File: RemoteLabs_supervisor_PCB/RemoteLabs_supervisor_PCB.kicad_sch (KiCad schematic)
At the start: 20 parts, among them J1 Super_Prog_Header, J2 WS2821B Header, J26 Student_Prog_Header, J27 Analog Buffer

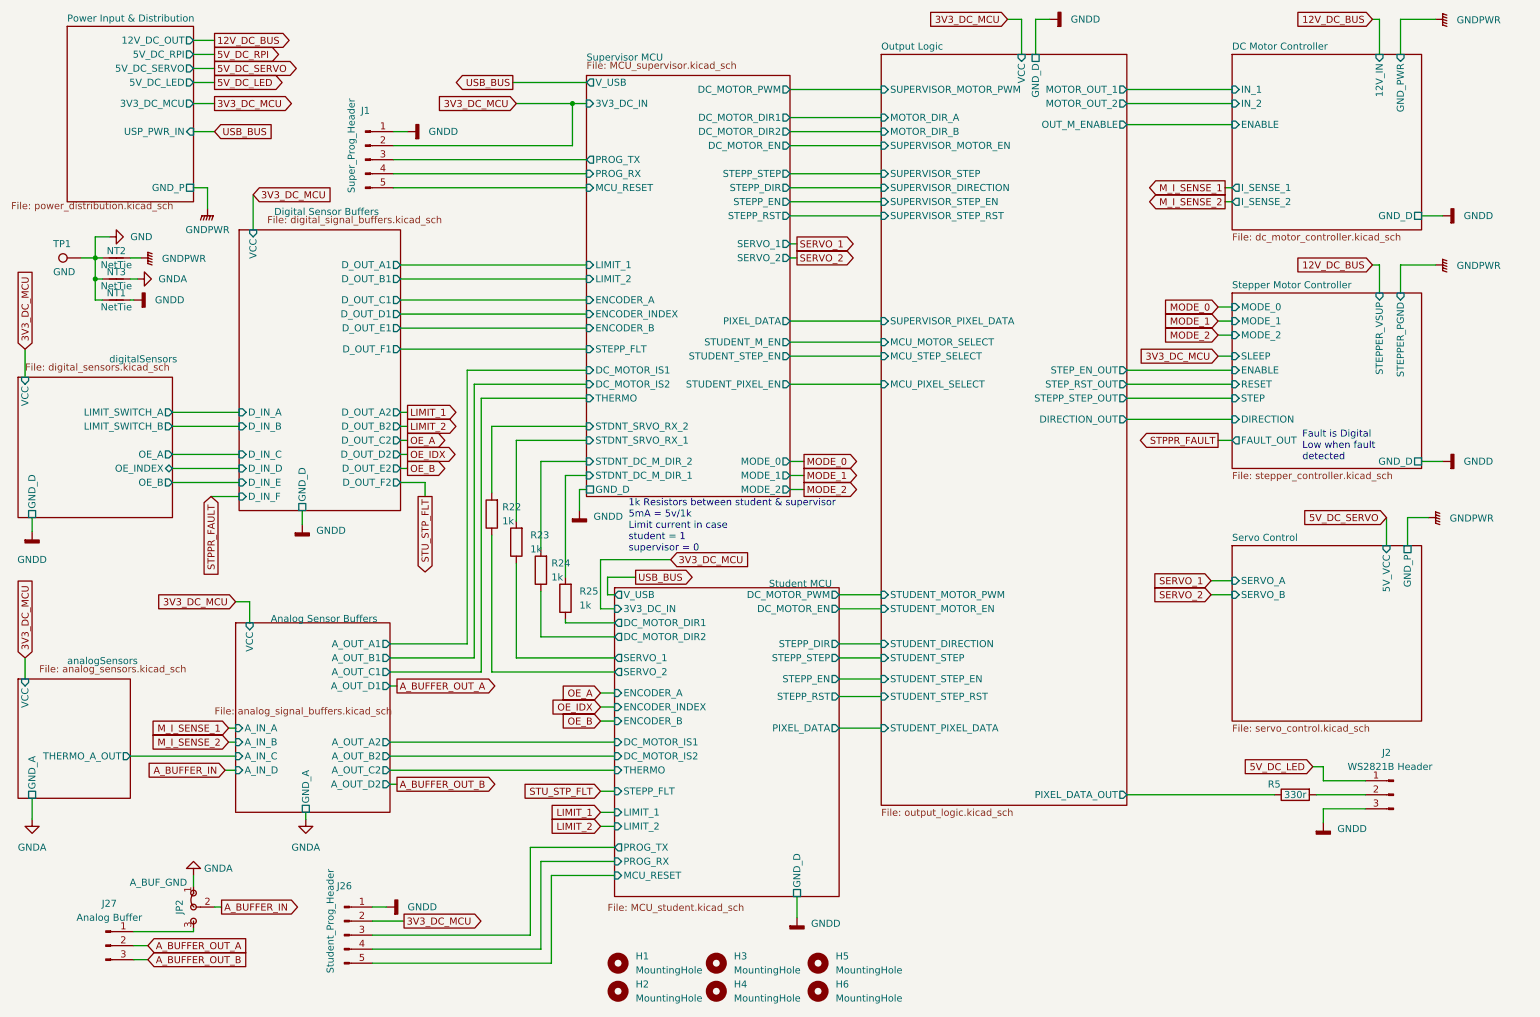
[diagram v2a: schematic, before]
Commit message: version one finished excluding net ties
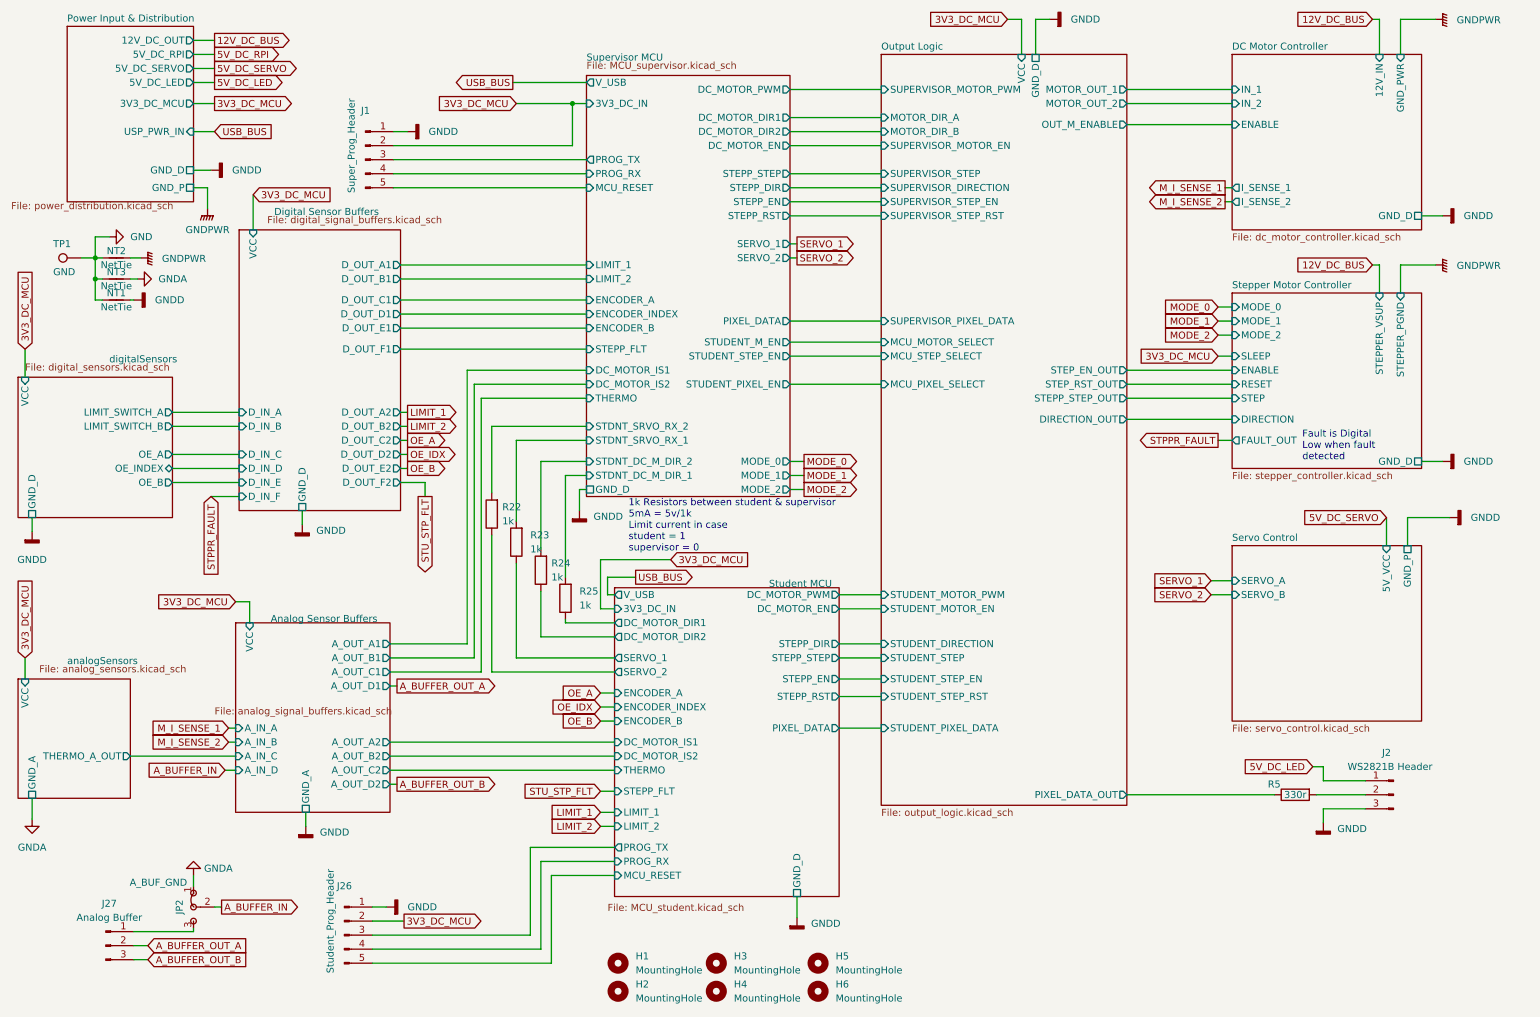
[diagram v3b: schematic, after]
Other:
- sheet Power Input & Distribution ports: added GND_D; removed none
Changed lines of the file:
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@@
+    (stroke (width 0) (type default) (color 0 0 0 0))
+  )
+  (wire (pts (xy 66.04 160.02) (xy 66.04 162.56))
     (stroke (width 0) (type default) (color 0 0 0 0))
   )
@@
     (stroke (width 0) (type default) (color 0 0 0 0))
   )
+  (wire (pts (xy 45.72 43.815) (xy 48.895 43.815))
+    (stroke (width 0) (type default) (color 0 0 0 0))
+  )
   (wire (pts (xy 231.14 92.71) (xy 233.68 92.71))
     (stroke (width 0) (type default) (color 0 0 0 0))
@@
     (stroke (width 0) (type default) (color 0 0 0 0))
   )
-  (wire (pts (xy 269.24 106.68) (xy 265.43 106.68))
+  (wire (pts (xy 265.43 106.68) (xy 273.05 106.68))
     (stroke (width 0) (type default) (color 0 0 0 0))
   )
@@
   )
   (wire (pts (xy 15.24 76.2) (xy 15.24 81.28))
-    (stroke (width 0) (type default) (color 0 0 0 0))
-  )
-  (wire (pts (xy 66.04 160.02) (xy 66.04 161.29))
     (stroke (width 0) (type default) (color 0 0 0 0))
   )
@@
       (effects (font (size 1.27 1.27)) (justify left) hide)
     )
-  )
-  (symbol (lib_id "power:GNDPWR") (at 269.24 106.68 90) (unit 1)
-    (in_bom yes) (on_board yes) (fields_autoplaced)
-    (property "Reference" "#PWR014" (id 0) (at 274.32 106.68 0)
-      (effects (font (size 1.27 1.27)) hide)
-    )
-    (property "Value" "GNDPWR" (id 1) (at 273.05 106.8069 90)
-      (effects (font (size 1.27 1.27)) (justify right))
-    )
-    (property "Footprint" "" (id 2) (at 270.51 106.68 0)
-      (effects (font (size 1.27 1.27)) hide)
-    )
-    (property "Datasheet" "" (id 3) (at 270.51 106.68 0)
-      (effects (font (size 1.27 1.27)) hide)
-    )
-    (pin "1")
   )
   (symbol (lib_id "Connector:Conn_01x03_Male") (at 29.845 184.15 0) (unit 1)
@@
     (pin "2")
   )
+  (symbol (lib_id "power:GNDD") (at 273.05 106.68 90) (unit 1)
+    (in_bom yes) (on_board yes) (fields_autoplaced)
+    (property "Reference" "#PWR0103" (id 0) (at 279.4 106.68 0)
+      (effects (font (size 1.27 1.27)) hide)
+    )
+    (property "Value" "GNDD" (id 1) (at 276.86 106.6799 90)
+      (effects (font (size 1.27 1.27)) (justify right))
+    )
+    (property "Footprint" "" (id 2) (at 273.05 106.68 0)
+      (effects (font (size 1.27 1.27)) hide)
+    )
+    (property "Datasheet" "" (id 3) (at 273.05 106.68 0)
+      (effects (font (size 1.27 1.27)) hide)
+    )
+    (pin "1")
+  )
   (symbol (lib_id "power:GNDD") (at 84.455 36.83 90) (unit 1)
     (in_bom yes) (on_board yes) (fields_autoplaced)
@@
     (pin "1")
   )
+  (symbol (lib_id "power:GNDD") (at 66.04 162.56 0) (unit 1)
+    (in_bom yes) (on_board yes) (fields_autoplaced)
+    (property "Reference" "#PWR?" (id 0) (at 66.04 168.91 0)
+      (effects (font (size 1.27 1.27)) hide)
+    )
+    (property "Value" "GNDD" (id 1) (at 68.58 163.6394 0)
+      (effects (font (size 1.27 1.27)) (justify left))
+    )
+    (property "Footprint" "" (id 2) (at 66.04 162.56 0)
+      (effects (font (size 1.27 1.27)) hide)
+    )
+    (property "Datasheet" "" (id 3) (at 66.04 162.56 0)
+      (effects (font (size 1.27 1.27)) hide)
+    )
+    (pin "1")
+  )
   (symbol (lib_id "Mechanical:MountingHole_M3") (at 140.335 192.405 0) (unit 1)
     (in_bom yes) (on_board yes) (fields_autoplaced)
@@
     (pin "2")
   )
-  (symbol (lib_id "power:GNDA") (at 66.04 161.29 0) (unit 1)
-    (in_bom yes) (on_board yes) (fields_autoplaced)
-    (property "Reference" "#PWR09" (id 0) (at 66.04 167.64 0)
-      (effects (font (size 1.27 1.27)) hide)
-    )
-    (property "Value" "GNDA" (id 1) (at 66.04 166.37 0))
-    (property "Footprint" "" (id 2) (at 66.04 161.29 0)
-      (effects (font (size 1.27 1.27)) hide)
-    )
-    (property "Datasheet" "" (id 3) (at 66.04 161.29 0)
-      (effects (font (size 1.27 1.27)) hide)
-    )
-    (pin "1")
-  )
   (symbol (lib_id "Mechanical:MountingHole_M3") (at 158.75 187.325 0) (unit 1)
     (in_bom yes) (on_board yes) (fields_autoplaced)
@@
     (pin "1")
     (pin "2")
+  )
+  (symbol (lib_id "power:GNDD") (at 48.895 43.815 90) (unit 1)
+    (in_bom yes) (on_board yes) (fields_autoplaced)
+    (property "Reference" "#PWR0102" (id 0) (at 55.245 43.815 0)
+      (effects (font (size 1.27 1.27)) hide)
+    )
+    (property "Value" "GNDD" (id 1) (at 52.705 43.8149 90)
+      (effects (font (size 1.27 1.27)) (justify right))
+    )
+    (property "Footprint" "" (id 2) (at 48.895 43.815 0)
+      (effects (font (size 1.27 1.27)) hide)
+    )
+    (property "Datasheet" "" (id 3) (at 48.895 43.815 0)
+      (effects (font (size 1.27 1.27)) hide)
+    )
+    (pin "1")
   )
   (symbol (lib_id "000_Resistors_Immo:Resistor_0805") (at 245.11 156.845 0) (mirror x) (unit 1)
@@
     )
     (pin "5V_DC_LED" output (at 45.72 27.94 0)
+      (effects (font (size 1.27 1.27)) (justify right))
+    )
+    (pin "GND_D" passive (at 45.72 43.815 0)
       (effects (font (size 1.27 1.27)) (justify right))
     )
@@
       (reference "#PWR08") (unit 1) (value "GNDD") (footprint "")
     )
-    (path "/c61aa19b-572b-447e-9c21-fb7798e74949"
-      (reference "#PWR09") (unit 1) (value "GNDA") (footprint "")
-    )
     (path "/3fedc316-aba4-4db2-a001-9e9f592154c4"
       (reference "#PWR010") (unit 1) (value "GNDD") (footprint "")
@@
       (reference "#PWR013") (unit 1) (value "GNDD") (footprint "")
     )
-    (path "/0e1f21ff-22d6-42a8-bc60-da4828a62a09"
-      (reference "#PWR014") (unit 1) (value "GNDPWR") (footprint "")
-    )
     (path "/9065d0c8-3ffe-4c30-b2a6-e42a28937b37"
       (reference "#PWR015") (unit 1) (value "GNDPWR") (footprint "")
@@
       (reference "#PWR0101") (unit 1) (value "GNDA") (footprint "")
     )
+    (path "/d2f72cbc-e1a3-49c0-b76e-d4b4cbb83949"
+      (reference "#PWR0102") (unit 1) (value "GNDD") (footprint "")
+    )
+    (path "/3bac50b7-56a3-4968-b3cc-377a7f23162c"
+      (reference "#PWR0103") (unit 1) (value "GNDD") (footprint "")
+    )
+    (path "/689ebb8c-51ab-4e32-9841-0bcb9e801411"
+      (reference "#PWR?") (unit 1) (value "GNDD") (footprint "")
+    )
     (path "/ef79b516-f387-4bff-98aa-61eff96e72d2/38b234c4-9ac0-49c1-96ba-77416ddaece9"

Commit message: routing board layout 2.0
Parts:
- removed TP1: GND, TestPoint:TestPoint_Pad_D1.5mm, symbol Connector:TestPoint

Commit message: Version 2 PCB Layout
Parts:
- removed NT3: NetTie, NetTie:NetTie-2_SMD_Pad0.5mm, symbol Device:NetTie_2
- NT1: footprint NetTie:NetTie-2_SMD_Pad0.5mm -> NetTie:NetTie-2_SMD_Pad2.0mm
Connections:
- net GNDD: now also NT1.1; no longer NT1.2
- net GNDPWR: now also NT1.2
- net GND renamed GND_PB
- net GND_PB: no longer NT1.1
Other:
- sheet Power Input & Distribution ports: added GND_PB; removed none
- moved on the sheet: NT2

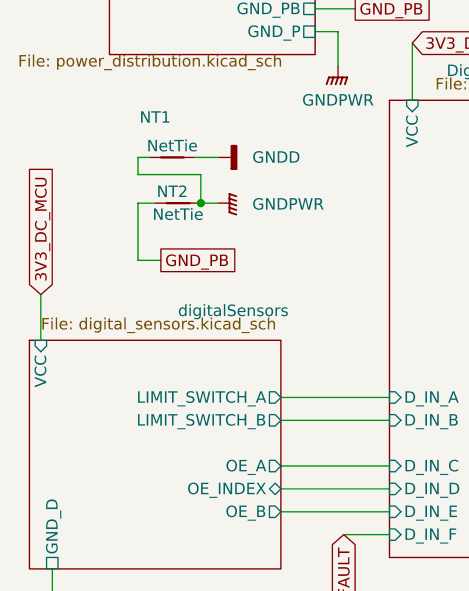
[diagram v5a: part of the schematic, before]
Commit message: Test software mostly tested - awaiting hardware
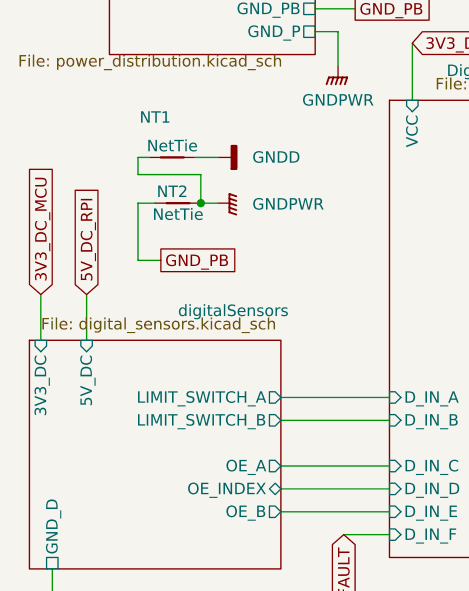
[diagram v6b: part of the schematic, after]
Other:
- sheet digitalSensors ports: added 3V3_DC, 5V_DC; removed VCC
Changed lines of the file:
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@@
+    (stroke (width 0) (type default) (color 0 0 0 0))
+  )
+  (wire (pts (xy 20.32 76.2) (xy 20.32 81.28))
     (stroke (width 0) (type default) (color 0 0 0 0))
   )
@@
     (effects (font (size 1.27 1.27)) (justify left))
     (property "Intersheet References" "${INTERSHEET_REFS}" (id 0) (at 165.5779 59.6106 0)
+      (effects (font (size 1.27 1.27)) (justify left) hide)
+    )
+  )
+  (global_label "5V_DC_RPI" (shape input) (at 20.32 76.2 90) (fields_autoplaced)
+    (effects (font (size 1.27 1.27)) (justify left))
+    (property "Intersheet References" "${INTERSHEET_REFS}" (id 0) (at 20.2406 63.8688 90)
       (effects (font (size 1.27 1.27)) (justify left) hide)
     )
@@
       (effects (font (size 1.27 1.27)) (justify right))
     )
-    (pin "VCC" input (at 15.24 81.28 90)
-      (effects (font (size 1.27 1.27)) (justify right))
-    )
     (pin "GND_D" passive (at 16.51 106.68 270)
       (effects (font (size 1.27 1.27)) (justify left))
@@
       (effects (font (size 1.27 1.27)) (justify right))
     )
+    (pin "3V3_DC" input (at 15.24 81.28 90)
+      (effects (font (size 1.27 1.27)) (justify right))
+    )
+    (pin "5V_DC" input (at 20.32 81.28 90)
+      (effects (font (size 1.27 1.27)) (justify right))
+    )

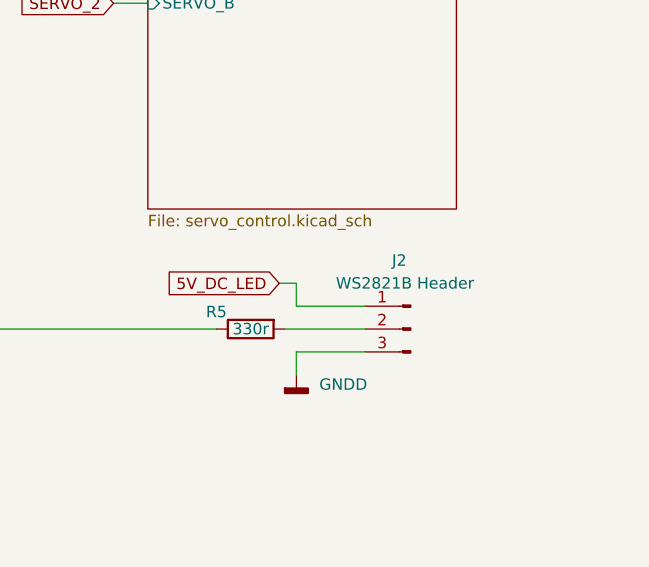
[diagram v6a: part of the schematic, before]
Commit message: Edited PCB design for V1.1
- Changed pin sizes for stepper motor
- Change pin sizes for DC/DC Buck module.
- In process of changing text to be readable by human beings
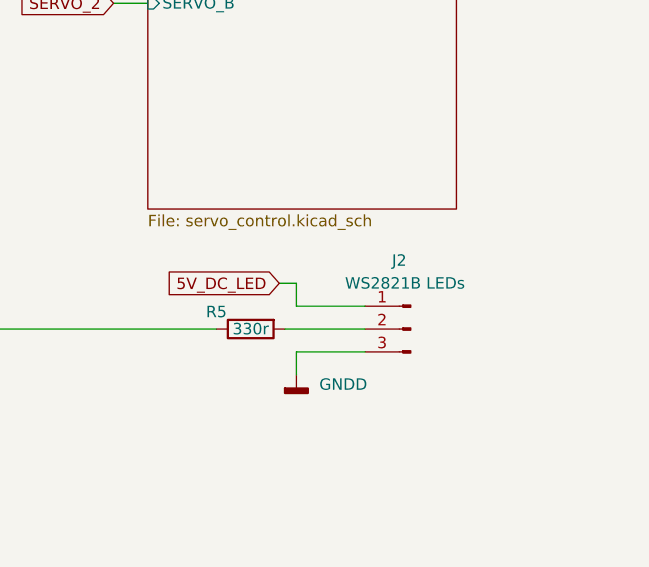
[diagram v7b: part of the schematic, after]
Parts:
- J2: value WS2821B Header -> WS2821B LEDs
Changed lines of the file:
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@@
     (in_bom yes) (on_board yes)
     (property "Reference" "J2" (id 0) (at 261.62 149.225 0))
-    (property "Value" "WS2821B Header" (id 1) (at 262.255 151.765 0))
+    (property "Value" "WS2821B LEDs" (id 1) (at 262.255 151.765 0))
     (property "Footprint" "Connector_Molex:Molex_KK-254_AE-6410-03A_1x03_P2.54mm_Vertical" (id 2) (at 259.461 163.83 0)
       (effects (font (size 1.27 1.27)) hide)
@@
     )
     (path "/9f02ea00-3ee8-4183-95b6-7d59f1944b3b"
-      (reference "J2") (unit 1) (value "WS2821B Header") (footprint "Connector_Molex:Molex_KK-254_AE-6410-03A_1x03_P2.54mm_Vertical")
+      (reference "J2") (unit 1) (value "WS2821B LEDs") (footprint "Connector_Molex:Molex_KK-254_AE-6410-03A_1x03_P2.54mm_Vertical")
     )
     (path "/586ec748-563a-478a-82db-706fb951336a/3d412b69-c529-4e16-8a2a-e7a8b0ecba07"
@@
     )
     (path "/9266ad98-56ad-4979-a534-eef1d9b8c163/a114a11f-bfc4-4928-86c4-97c65a6ed20e"
-      (reference "J16") (unit 1) (value "MotorController_PWR_IP") (footprint "TerminalBlock:TerminalBlock_Altech_AK300-2_P5.00mm")
+      (reference "J16") (unit 1) (value "DC Motor PWR") (footprint "TerminalBlock:TerminalBlock_Altech_AK300-2_P5.00mm")
     )
     (path "/9266ad98-56ad-4979-a534-eef1d9b8c163/5af9da8d-e47c-420a-916a-caa63524047f"
-      (reference "J17") (unit 1) (value "MotorController") (footprint "TerminalBlock:TerminalBlock_Altech_AK300-3_P5.00mm")
+      (reference "J17") (unit 1) (value "MotorController Output") (footprint "TerminalBlock:TerminalBlock_Altech_AK300-3_P5.00mm")
     )
     (path "/9266ad98-56ad-4979-a534-eef1d9b8c163/a5bbde6e-7d19-4d22-b40b-936aabc1c3ee"
@@
     )
     (path "/283d3eb1-906d-460d-a87d-d328f41afedd/32542479-583c-4860-855d-1a981b7c2a95"
-      (reference "J22") (unit 1) (value "Thermocouple A") (footprint "TerminalBlock:TerminalBlock_Altech_AK300-2_P5.00mm")
+      (reference "J22") (unit 1) (value "Thermocouple") (footprint "TerminalBlock:TerminalBlock_Altech_AK300-2_P5.00mm")
     )
     (path "/3053d1d3-1dd5-4dac-b6cb-5e7828c7a42e/dced00b5-ead7-46bd-ad39-3400c2dba3fa"
@@
     )
     (path "/0d587a0a-c67c-4fed-9eec-791a57f2bb2e/26e9e77b-c4f0-439a-94a1-c5ad551b03df"
-      (reference "JP9") (unit 1) (value "Reset Jumper") (footprint "000_Connectors_Immo:SolderJumper-2_P1.3mm_Open_Pad1.0x1.5mm")
+      (reference "JP9") (unit 1) (value "Reset GND") (footprint "000_Connectors_Immo:SolderJumper-2_P1.3mm_Open_Pad1.0x1.5mm")
     )
     (path "/ef79b516-f387-4bff-98aa-61eff96e72d2/27c64e6c-34e2-4309-a9fd-258ec95a64a3"
-      (reference "JP10") (unit 1) (value "Reset Jumper") (footprint "000_Connectors_Immo:SolderJumper-2_P1.3mm_Open_Pad1.0x1.5mm")
+      (reference "JP10") (unit 1) (value "Reset GND") (footprint "000_Connectors_Immo:SolderJumper-2_P1.3mm_Open_Pad1.0x1.5mm")
     )
     (path "/e22ce5dc-891a-4dca-b3d5-9b5457b27dd4"
@@
     )
     (path "/ef79b516-f387-4bff-98aa-61eff96e72d2/c3d7271c-6e47-4f7e-9640-bbb0cbe0a9ed"
-      (reference "X1") (unit 1) (value "ASEK-xxxMHz") (footprint "Oscillator:Oscillator_SMD_Abracon_ASE-4Pin_3.2x2.5mm")
+      (reference "X1") (unit 1) (value "32.768kHz") (footprint "Oscillator:Oscillator_SMD_Abracon_ASE-4Pin_3.2x2.5mm")
     )
     (path "/0d587a0a-c67c-4fed-9eec-791a57f2bb2e/c3e3fe82-191d-4b68-a413-86f5473afb26"
-      (reference "X2") (unit 1) (value "ASEK-xxxMHz") (footprint "Oscillator:Oscillator_SMD_Abracon_ASE-4Pin_3.2x2.5mm")
-    )
-  )
+      (reference "X2") (unit 1) (value "32.768kHz") (footprint "Oscillator:Oscillator_SMD_Abracon_ASE-4Pin_3.2x2.5mm")
+    )
+  )
